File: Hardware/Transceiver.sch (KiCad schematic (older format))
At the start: 1 part

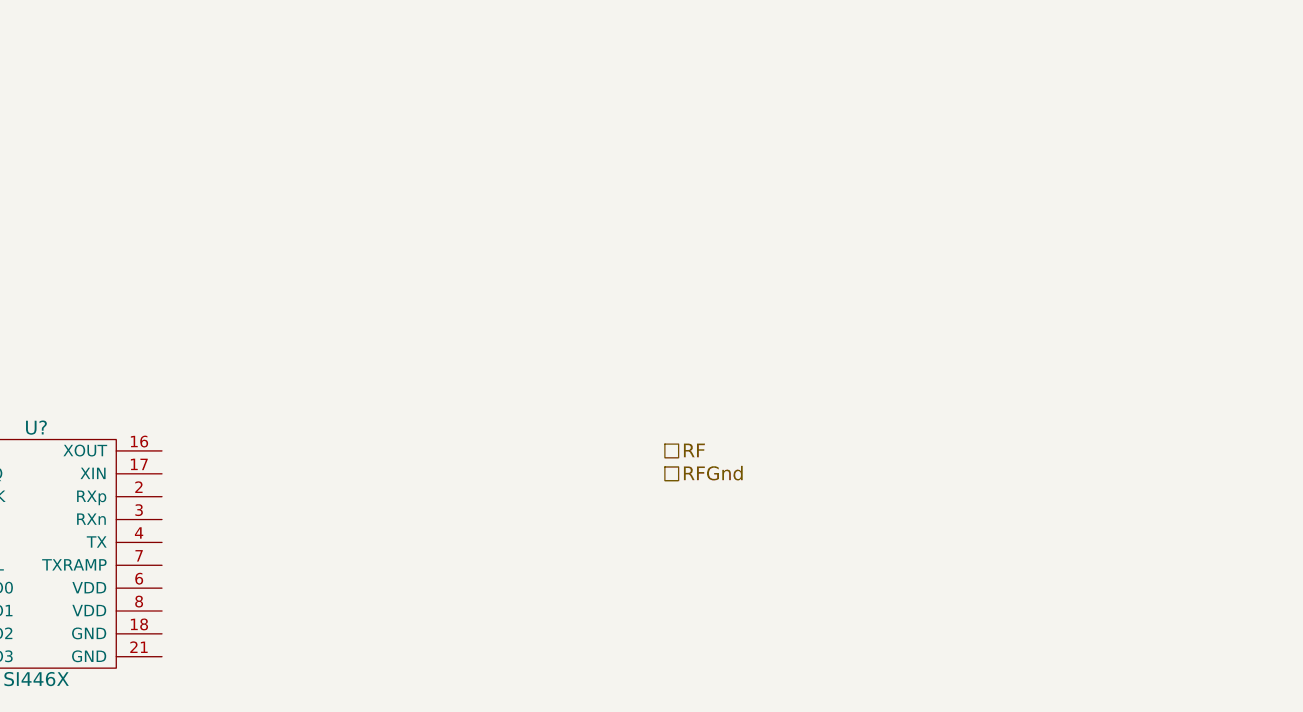
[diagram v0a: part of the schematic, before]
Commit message: RX signal chain topology
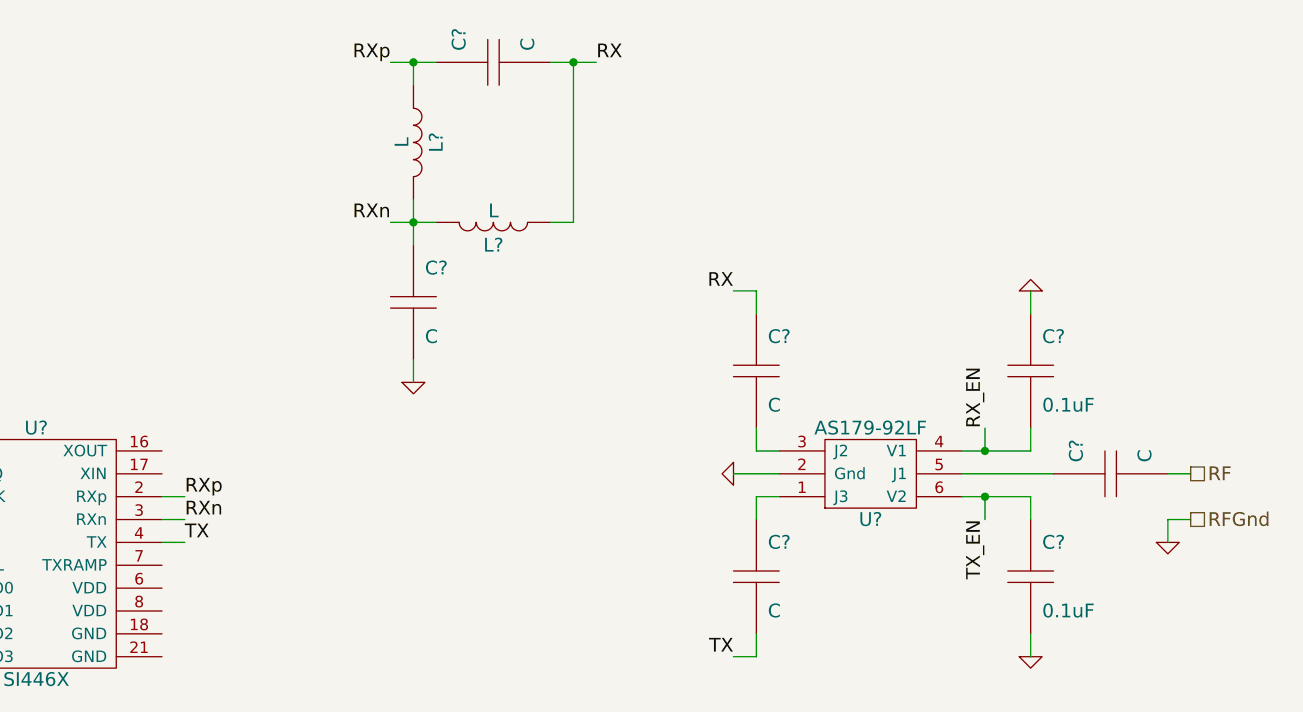
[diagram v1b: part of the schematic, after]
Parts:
- added C? (x5): C, ~, symbol C
- added C? (x2): 0.1uF, ~, symbol C
- added L? (x2): L, ~, symbol L
- added U?: AS179-92LF, symbol AS179-92LF
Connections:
- net RF: now also C?.2
- net RXp: now reaches U?.2 (RXp)
- net RXp: now also C?.1, L?.2
- net RXn: now reaches U?.3 (RXn)
- net RXn: now also C?.1, L?.1, L?.1
- net TX: now reaches U?.4 (TX)
- net TX: now also C?.2
- new net: C?.1, U?.1 (J3)
- new net: C?.2, U?.3 (J2)
- new net: C?.1, U?.5 (J1)
- new net GND: C?.1, C?.2, C?.2, U?.2 (Gnd)
- new net RX: C?.1, C?.2, L?.2
- new net RX_EN: C?.2, U?.4 (V1)
- new net TX_EN: C?.1, U?.6 (V2)

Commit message: Add LO
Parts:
- added C? (x2): 0.1uF, ~, symbol C
- added Q?: VCXO, ~, symbol VCXO
- added R? (x3): R, ~, symbol R
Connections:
- net CS: now also U?.15 (nSEL)
- net GND: now also C?.2, C?.2, Q?.3 (Gnd), R?.1, R?.1
- net MISO: now also U?.13 (SDO)
- net MOSI: now also U?.14 (SDI)
- net SCLK: now also U?.12 (SCLK)
- net LO: now reaches U?.17 (XIN)
- net LO: now also R?.2, R?.2
- net TX renamed TX1
- net TX1: no longer C?.2
- new net: Q?.4 (Out), R?.1, R?.2
- new net +3.3V: C?.1, Q?.6 (Vdd)
- new net LO_EN: Q?.2 (En)
- new net Mod: C?.1, Q?.1 (VC)
- new net TX2: C?.2
- no-connect marks 0 -> 1
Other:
- note added: "VCXO Out - 10%-90%\nLO Input - 1.4 p-p AC"
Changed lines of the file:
@@
 $Descr A4 11693 8268
 encoding utf-8
-Sheet 4 4
+Sheet 4 5
 Title "Aether - Pico Tracker"
-Date "31 jul 2014"
+Date "2 aug 2014"
 Rev "1"
 Comp "Aerodyne Labs"
@@
 RXn
 Text Label 6200 3300 0    60   ~ 0
-TX
+TX1
 Wire Wire Line
 	6100 3100 6200 3100
@@
 	8700 2200 8700 2300
 Text Label 8600 3800 2    60   ~ 0
-TX
+TX2
 Wire Wire Line
 	8600 3800 8700 3800
@@
 RX
 Connection ~ 7900 1200
+$Comp
+L VCXO Q?
+U 1 1 53DC5D94
+P 4800 5400
+F 0 "Q?" H 4800 5600 60  0000 C CNN
+F 1 "VCXO" H 4800 5200 60  0000 C CNN
+F 2 "~" H 4800 5400 60  0000 C CNN
+F 3 "~" H 4800 5400 60  0000 C CNN
+	1    4800 5400
+	1    0    0    -1
+$EndComp
+$Comp
+L C C?
+U 1 1 53DC5DA3
+P 4100 5850
+F 0 "C?" H 4150 6000 60  0000 L CNN
+F 1 "0.1uF" H 4150 5700 60  0000 L CNN
+F 2 "~" H 4100 5850 60  0000 C CNN
+F 3 "~" H 4100 5850 60  0000 C CNN
+F 4 "V" H 4050 5700 60  0001 R CNN "Voltage"
+F 5 "D" H 4050 6000 60  0001 R CNN "Dielectric"
+	1    4100 5850
+	1    0    0    -1
+$EndComp
+$Comp
+L C C?
+U 1 1 53DC5DC5
+P 3700 5850
+F 0 "C?" H 3750 6000 60  0000 L CNN
+F 1 "0.1uF" H 3750 5700 60  0000 L CNN
+F 2 "~" H 3700 5850 60  0000 C CNN
+F 3 "~" H 3700 5850 60  0000 C CNN
+F 4 "V" H 3650 5700 60  0001 R CNN "Voltage"
+F 5 "D" H 3650 6000 60  0001 R CNN "Dielectric"
+	1    3700 5850
+	1    0    0    -1
+$EndComp
+$Comp
+L +3.3V #PWR?
+U 1 1 53DC5DCD
+P 4100 5200
+F 0 "#PWR?" H 4100 5160 30  0001 C CNN
+F 1 "+3.3V" H 4100 5310 30  0000 C CNN
+F 2 "" H 4100 5200 60  0000 C CNN
+F 3 "" H 4100 5200 60  0000 C CNN
+	1    4100 5200
+	1    0    0    -1
+$EndComp
+Wire Wire Line
+	4100 5200 4100 5600
+Wire Wire Line
+	4200 5500 4100 5500
+Connection ~ 4100 5500
+Text HLabel 3600 5300 0    60   Input ~ 0
+Mod
+Wire Wire Line
+	3600 5300 4200 5300
+Wire Wire Line
+	3700 5600 3700 5300
+Connection ~ 3700 5300
+$Comp
+L GND #PWR?
+U 1 1 53DC5E7C
+P 4100 6200
+F 0 "#PWR?" H 4100 6200 30  0001 C CNN
+F 1 "GND" H 4100 6130 30  0001 C CNN
+F 2 "" H 4100 6200 60  0000 C CNN
+F 3 "" H 4100 6200 60  0000 C CNN
+	1    4100 6200
+	1    0    0    -1
+$EndComp
+$Comp
+L GND #PWR?
+U 1 1 53DC5E8B
+P 3700 6200
+F 0 "#PWR?" H 3700 6200 30  0001 C CNN
+F 1 "GND" H 3700 6130 30  0001 C CNN
+F 2 "" H 3700 6200 60  0000 C CNN
+F 3 "" H 3700 6200 60  0000 C CNN
+	1    3700 6200
+	1    0    0    -1
+$EndComp
+$Comp
+L GND #PWR?
+U 1 1 53DC5E9A
+P 5500 5600
+F 0 "#PWR?" H 5500 5600 30  0001 C CNN
+F 1 "GND" H 5500 5530 30  0001 C CNN
+F 2 "" H 5500 5600 60  0000 C CNN
+F 3 "" H 5500 5600 60  0000 C CNN
+	1    5500 5600
+	1    0    0    -1
+$EndComp
+Wire Wire Line
+	5400 5500 5500 5500
+Wire Wire Line
+	5500 5500 5500 5600
+Wire Wire Line
+	3700 6100 3700 6200
+Wire Wire Line
+	4100 6100 4100 6200
+$Comp
+L R R?
+U 1 1 53DC5F32
+P 5800 5750
+F 0 "R?" H 5800 5850 50  0000 C CNN
+F 1 "R" H 5800 5750 50  0000 C CNN
+F 2 "~" H 5800 5750 60  0000 C CNN
+F 3 "~" H 5800 5750 60  0000 C CNN
+F 4 "W" H 5800 5650 50  0001 C CNN "Power"
+F 5 "%" H 5800 5550 50  0001 C CNN "Tolerance"
+	1    5800 5750
+	0    -1   -1   0
+$EndComp
+$Comp
+L R R?
+U 1 1 53DC5F4D
+P 6150 5400
+F 0 "R?" H 6150 5500 50  0000 C CNN
+F 1 "R" H 6150 5400 50  0000 C CNN
+F 2 "~" H 6150 5400 60  0000 C CNN
+F 3 "~" H 6150 5400 60  0000 C CNN
+F 4 "W" H 6150 5300 50  0001 C CNN "Power"
+F 5 "%" H 6150 5200 50  0001 C CNN "Tolerance"
+	1    6150 5400
+	1    0    0    -1
+$EndComp
+$Comp
+L R R?
+U 1 1 53DC5F68
+P 6500 5750
+F 0 "R?" H 6500 5850 50  0000 C CNN
+F 1 "R" H 6500 5750 50  0000 C CNN
+F 2 "~" H 6500 5750 60  0000 C CNN
+F 3 "~" H 6500 5750 60  0000 C CNN
+F 4 "W" H 6500 5650 50  0001 C CNN "Power"
+F 5 "%" H 6500 5550 50  0001 C CNN "Tolerance"
+	1    6500 5750
+	0    -1   -1   0
+$EndComp
+$Comp
+L GND #PWR?
+U 1 1 53DC5F83
+P 5800 6100
+F 0 "#PWR?" H 5800 6100 30  0001 C CNN
+F 1 "GND" H 5800 6030 30  0001 C CNN
+F 2 "" H 5800 6100 60  0000 C CNN
+F 3 "" H 5800 6100 60  0000 C CNN
+	1    5800 6100
+	1    0    0    -1
+$EndComp
+$Comp
+L GND #PWR?
+U 1 1 53DC5F92
+P 6500 6100
+F 0 "#PWR?" H 6500 6100 30  0001 C CNN
+F 1 "GND" H 6500 6030 30  0001 C CNN
+F 2 "" H 6500 6100 60  0000 C CNN
+F 3 "" H 6500 6100 60  0000 C CNN
+	1    6500 6100
+	1    0    0    -1
+$EndComp
+Text Label 6600 5400 0    60   ~ 0
+LO
+Wire Wire Line
+	6600 5400 6400 5400
+Wire Wire Line
+	6500 5500 6500 5400
+Connection ~ 6500 5400
+Wire Wire Line
+	6500 6000 6500 6100
+Wire Wire Line
+	5400 5400 5900 5400
+Wire Wire Line
+	5800 5500 5800 5400
+Connection ~ 5800 5400
+Wire Wire Line
+	5800 6000 5800 6100
+Text Label 6200 3000 0    60   ~ 0
+LO
+Wire Wire Line
+	6200 3000 6100 3000
+NoConn ~ 6100 2900
+Wire Wire Line
+	4700 3100 5000 3100
+Wire Wire Line
+	4700 3200 5000 3200
+Wire Wire Line
+	4700 3300 5000 3300
+Wire Wire Line
+	4700 3400 5000 3400
+Text HLabel 3600 5000 0    60   Input ~ 0
+LO_EN
+Wire Wire Line
+	3600 5000 5500 5000
+Wire Wire Line
+	5500 5000 5500 5300
+Wire Wire Line
+	5500 5300 5400 5300
+Text Notes 5600 5100 0    60   ~ 0
+VCXO Out - 10%-90%\nLO Input - 1.4 p-p AC
 $EndSCHEMATC

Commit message: Transceiver power control pins
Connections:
- net ~XCVR_EN: now reaches U?.1 (SDN)
- net XCVR_IRQ: now reaches U?.11 (nIRQ)
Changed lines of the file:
@@
 Text Notes 5600 5100 0    60   ~ 0
 VCXO Out - 10%-90%\nLO Input - 1.4 p-p AC
+Text HLabel 4700 2900 0    60   Input ~ 0
+~XCVR_EN
+Text HLabel 4700 3000 0    60   Output ~ 0
+XCVR_IRQ
+Wire Wire Line
+	4700 2900 5000 2900
+Wire Wire Line
+	4700 3000 5000 3000
 $EndSCHEMATC
